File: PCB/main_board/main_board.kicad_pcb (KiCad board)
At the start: 4 copper layers, 55.3 x 29 mm, 56 parts, among them CN1 XT30PW-M, CN2 XT30PW-M, U1 XT30PW-F, U2 W25Q32JVUUIQ, U3 W25N01GVZEIG_C907680, U4 INA226, U5 INA226, U6 RP2040, U7 AZ1117-3.3, X1 X322512MSB4SI

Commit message: Ready to JLC
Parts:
- added G***: LOGO, pcb_lib:OpenSourceHardware_3.5mm, F.Cu at (60.4, 27.0)
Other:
- board text added: "SC+Battery Current Sensor Board Author: Kelvin Zhao Version: V0.1 Design Date: Feb 2024"
- board text added: "SDA-BAT"
- board text added: "SDA-CAP"
- board text removed: "USB-C"

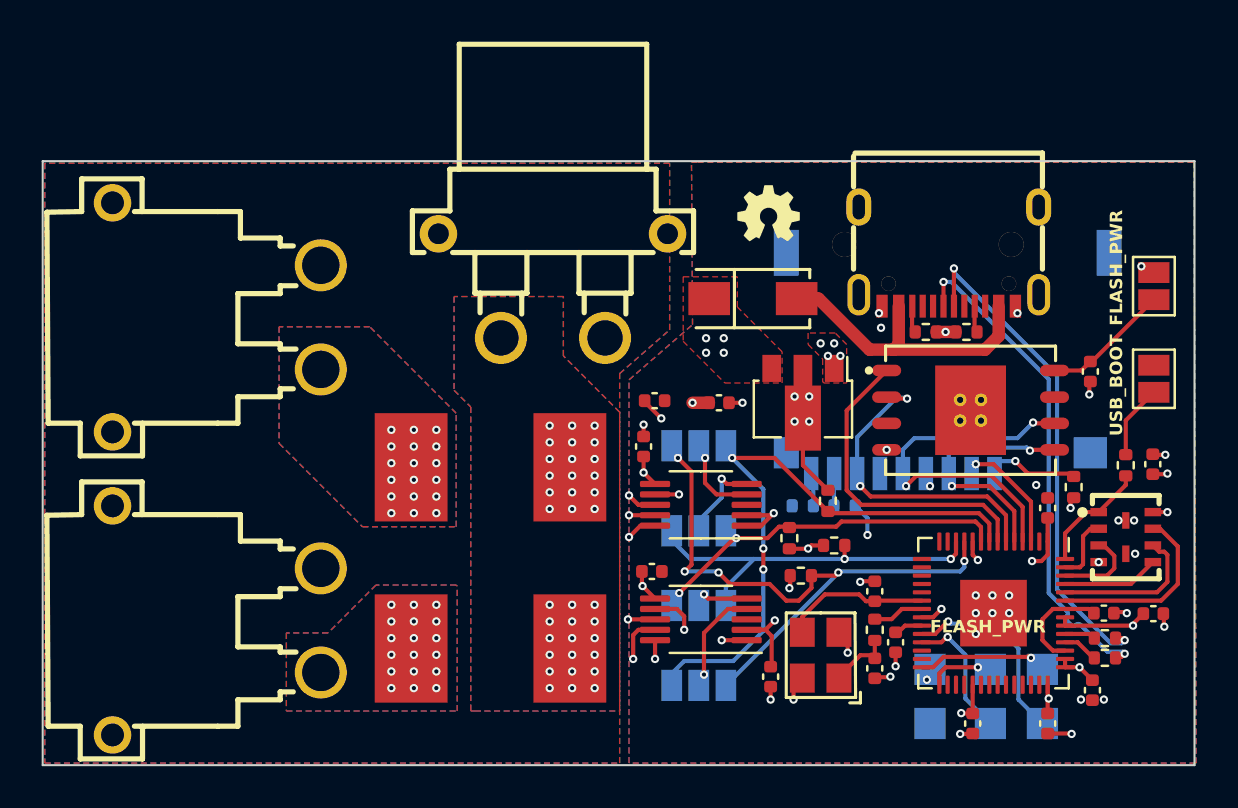
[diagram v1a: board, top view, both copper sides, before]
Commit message: Change LDO to BUCK converter
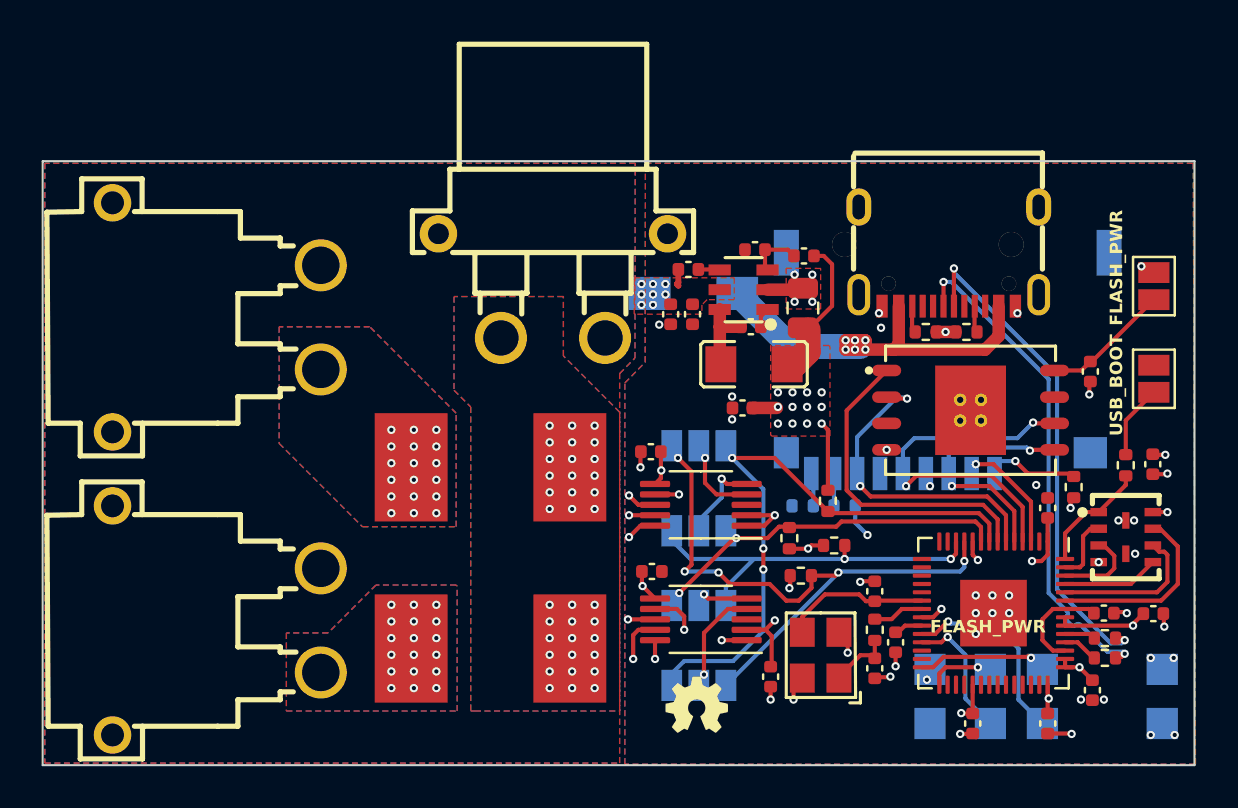
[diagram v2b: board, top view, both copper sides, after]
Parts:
- added C18: 0.1u, Capacitor_SMD:C_0402_1005Metric, F.Cu at (59.5, 32.5)
- added C19: 22u, Capacitor_SMD:C_0805_2012Metric, F.Cu at (62.0, 31.6)
- added C4: 0.1u, Capacitor_SMD:C_0402_1005Metric, F.Cu at (55.6, 31.9)
- added L1: CMP321609XD6R8MT, pcb_lib:L1206, F.Cu at (59.6, 34.2)
- added R3: 10k, Capacitor_SMD:C_0402_1005Metric, F.Cu at (56.5, 29.7)
- added R4: 51k, Capacitor_SMD:C_0402_1005Metric, F.Cu at (62.0, 29.1)
- added R5: 22.1k, Capacitor_SMD:C_0402_1005Metric, F.Cu at (59.7, 28.8)
- added TP7: 3.3, TestPoint:TestPoint_Pad_1.5x1.5mm, B.Cu at (79.2, 51.5)
- added TP8: GND, TestPoint:TestPoint_Pad_1.5x1.5mm, B.Cu at (79.2, 48.9)
- D1: moved to B.Cu
- U7: value AZ1117-3.3 -> TPS560430XDBVR; footprint Package_TO_SOT_SMD:SOT-89-3 -> pcb_lib:SOT-23-6_L2.9-W1.6-P0.95-LS2.8-BL
- moved G*** 23.9 mm to (56.9, 50.6)
- moved U7 6.40 mm to (59.2, 30.7), turned to 90 degrees
- moved C3 4.44 mm to (56.7, 31.9), turned to 90 degrees
- moved C12 4.23 mm to (59.1, 36.4), turned to 180 degrees
- moved D1 2.86 mm to (56.8, 30.9)
- moved C14 0.43 mm to (54.7, 38.5), turned to 180 degrees
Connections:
- C3 pad 1: IBAT+ -> GND
- C3 pad 2: GND -> IBAT+
- R14 pad 1: GND -> +3.3V
- U7 pad 1: GND -> Net-(U7-CB)
- U7 pad 2: +3.3V -> GND
- U7 pad 3: IBAT+ -> Net-(U7-FB)
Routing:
- net GND: track 45.5 -> 21.5 mm, vias 43 -> 46
- net VBUS: track 14.6 -> 20.1 mm, vias 0 -> 6
- net +3.3V: track 33.9 -> 39.2 mm, vias 22 -> 32
- net IBAT+: track 54.4 -> 50.0 mm, vias 25 -> 28
- net Net-(U7-SW): track 0.00 -> 3.64 mm
- net Net-(U7-FB): track 0.00 -> 2.39 mm
- net Net-(U7-EN): track 0.00 -> 1.03 mm
- net Net-(U7-CB): track 0.00 -> 0.96 mm
- added copper zone on F.Cu, net +3.3V
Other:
- board text added: "3V3"

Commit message: Ready for JLC for second time
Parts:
- moved G*** 0.92 mm to (56.1, 51.0)
- moved C12 0.80 mm to (59.0, 37.1)
- moved D1 0.76 mm to (57.5, 31.0)
- moved L1 0.65 mm to (59.6, 34.9)
- moved R5 0.32 mm to (59.8, 28.4)
- moved C18 0.30 mm to (59.5, 32.8)
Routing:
- net VBUS: track 20.1 -> 19.2 mm
- net Net-(U7-FB): track 2.39 -> 2.99 mm
- net +3.3V: track 39.2 -> 39.3 mm, vias 32 -> 28
- net IBAT+: vias 28 -> 25
- net GND: vias 46 -> 45
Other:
- board text added: "Open Source Hardware"

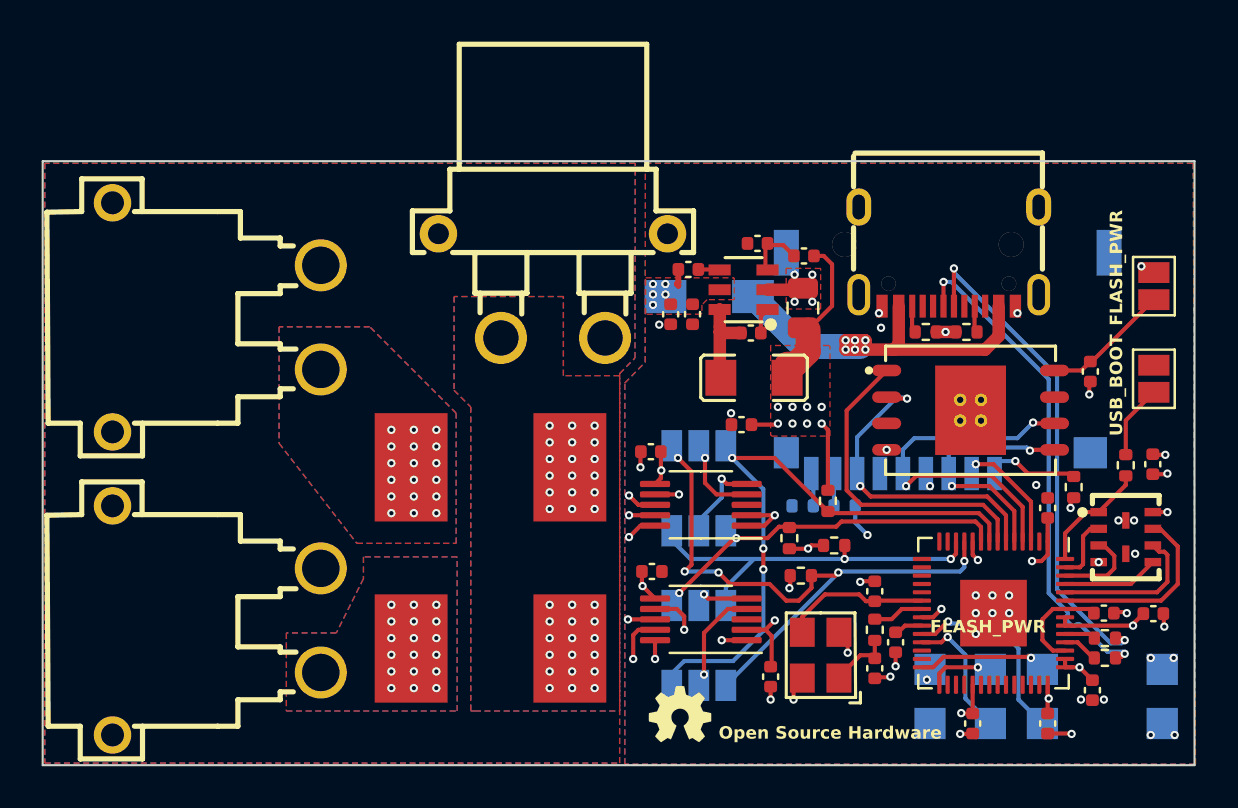
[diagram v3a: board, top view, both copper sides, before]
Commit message: Remove extra current carrier
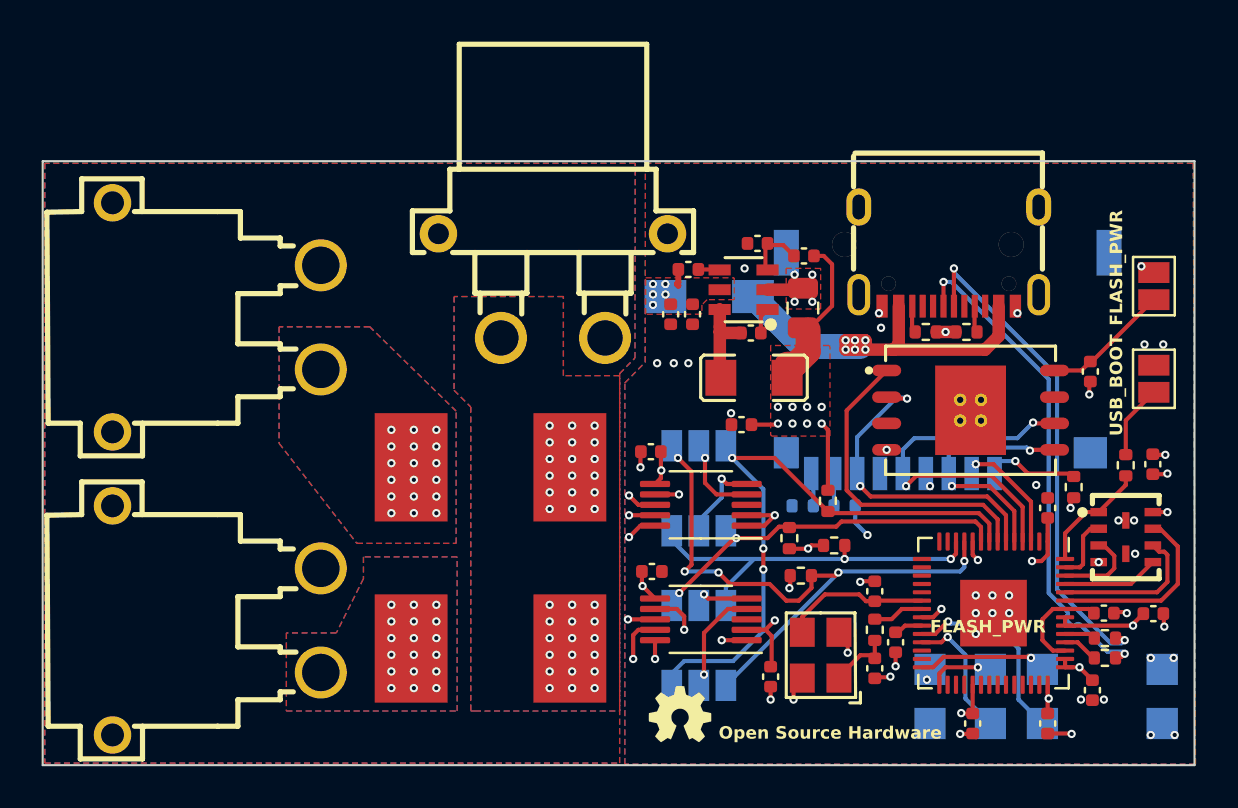
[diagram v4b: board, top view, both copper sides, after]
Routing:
- net GND: track 21.5 -> 31.3 mm, vias 45 -> 50
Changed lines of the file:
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@@
   (via (at 68.85 32.7) (size 0.4) (drill 0.2) (layers "F.Cu" "B.Cu") (free) (net 2))
   (via (at 66.45 48.75) (size 0.4) (drill 0.2) (layers "F.Cu" "B.Cu") (free) (net 2))
+  (via (at 56.5 34.2) (size 0.4) (drill 0.2) (layers "F.Cu" "B.Cu") (net 2))
   (via (at 58.55 36.6) (size 0.4) (drill 0.2) (layers "F.Cu" "B.Cu") (free) (net 2))
   (via (at 73.2 40.05) (size 0.4) (drill 0.2) (layers "F.Cu" "B.Cu") (free) (net 2))
   (via (at 79.4 38.6) (size 0.4) (drill 0.2) (layers "F.Cu" "B.Cu") (free) (net 2))
   (via (at 77.9 41.75) (size 0.4) (drill 0.2) (layers "F.Cu" "B.Cu") (free) (net 2))
+  (via (at 78.4 33.3) (size 0.4) (drill 0.2) (layers "F.Cu" "B.Cu") (free) (net 2))
   (via (at 71.9 46.2) (size 0.4) (drill 0.2) (layers "F.Cu" "B.Cu") (net 2))
   (via (at 75.75 35.7) (size 0.4) (drill 0.2) (layers "F.Cu" "B.Cu") (free) (net 2))
@@
   (via (at 56.3 47) (size 0.4) (drill 0.2) (layers "F.Cu" "B.Cu") (free) (net 2))
   (via (at 74.9 52) (size 0.4) (drill 0.2) (layers "F.Cu" "B.Cu") (free) (net 2))
+  (via (at 59.2 29.65) (size 0.4) (drill 0.2) (layers "F.Cu" "B.Cu") (free) (net 2))
   (via (at 67.95 49.4) (size 0.4) (drill 0.2) (layers "F.Cu" "B.Cu") (net 2))
   (via (at 66.02 38.36) (size 0.4) (drill 0.2) (layers "F.Cu" "B.Cu") (net 2))
@@
   (via (at 70.3 45.35) (size 0.4) (drill 0.2) (layers "F.Cu" "B.Cu") (net 2))
   (via (at 60.65 41.5) (size 0.4) (drill 0.2) (layers "F.Cu" "B.Cu") (free) (net 2))
-  (via (at 55.1 32.35) (size 0.4) (drill 0.2) (layers "F.Cu" "B.Cu") (net 2))
+  (via (at 55 34.2) (size 0.4) (drill 0.2) (layers "F.Cu" "B.Cu") (net 2))
   (via (at 78.7 48.35) (size 0.4) (drill 0.2) (layers "F.Cu" "B.Cu") (net 2))
   (via (at 65.75 32.5) (size 0.4) (drill 0.2) (layers "F.Cu" "B.Cu") (free) (net 2))
@@
   (via (at 61.6 31.25) (size 0.4) (drill 0.2) (layers "F.Cu" "B.Cu") (free) (net 2))
   (via (at 70.3 46.2) (size 0.4) (drill 0.2) (layers "F.Cu" "B.Cu") (net 2))
+  (via (at 79.3 33.3) (size 0.4) (drill 0.2) (layers "F.Cu" "B.Cu") (free) (net 2))
+  (via (at 55.8 34.2) (size 0.4) (drill 0.2) (layers "F.Cu" "B.Cu") (net 2))
   (via (at 79.35 46.85) (size 0.4) (drill 0.2) (layers "F.Cu" "B.Cu") (net 2))
+  (segment (start 52.5 32.9875) (end 59.8625 32.9875) (width 1.2) (layer "In1.Cu") (net 2))
+  (segment (start 59.8625 32.9875) (end 61.6 31.25) (width 1.2) (layer "In1.Cu") (net 2))
   (segment (start 39.2525 43.65) (end 38.8525 44.05) (width 0.2) (layer "In1.Cu") (net 2))
   (segment (start 55.95 30.4) (end 56 30.4) (width 0.286004) (layer "F.Cu") (net 3))
@@
         (xy 40.583332 42.85)
         (xy 45.35 42.85)
-        (xy 45.35 36.6)
+        (xy 45.35 36.5)
         (xy 41.2 32.45)
       )

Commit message: Add Custom ID
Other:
- board text added: "JLCJLCJLCJLC"
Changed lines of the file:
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@@
+    (effects (font (size 0.6 0.6) (thickness 0.1) bold) (justify left bottom mirror))
+  )
+  (gr_text "JLCJLCJLCJLC" (at 72.15 26.75) (layer "B.SilkS")
     (effects (font (size 0.6 0.6) (thickness 0.1) bold) (justify left bottom mirror))
   )

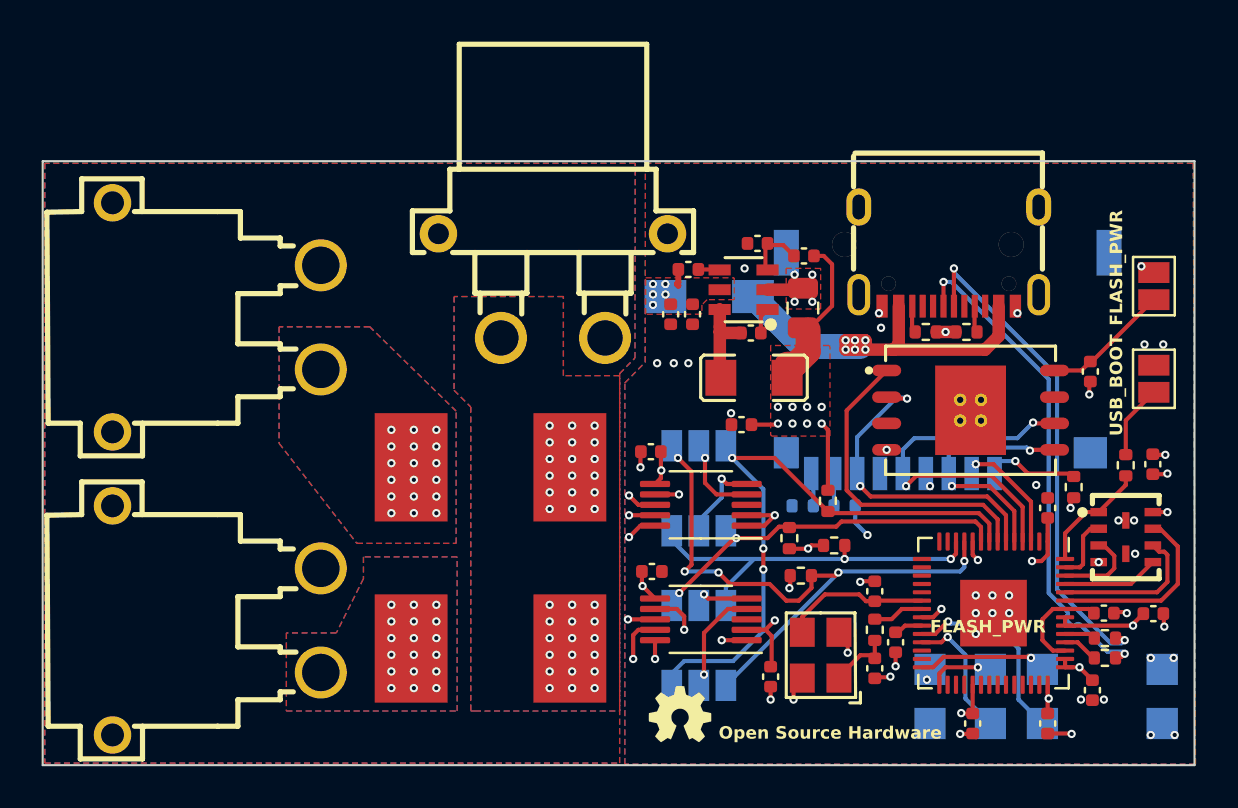
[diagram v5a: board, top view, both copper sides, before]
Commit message: Change vias drills to 0.3/0.5mm
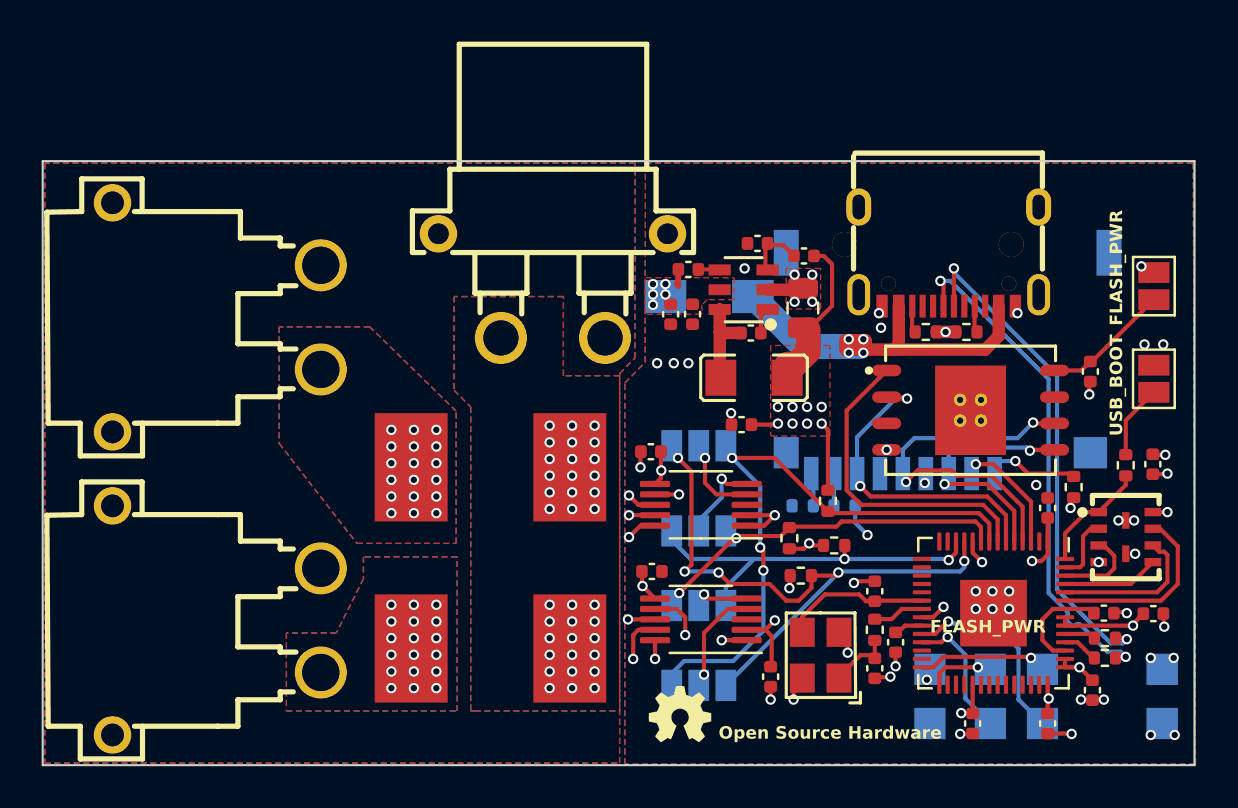
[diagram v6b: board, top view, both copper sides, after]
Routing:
- net GND: track 31.3 -> 31.9 mm, vias 50 -> 49
- net VBUS: vias 6 -> 4

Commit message: Change INA226 package for SMT
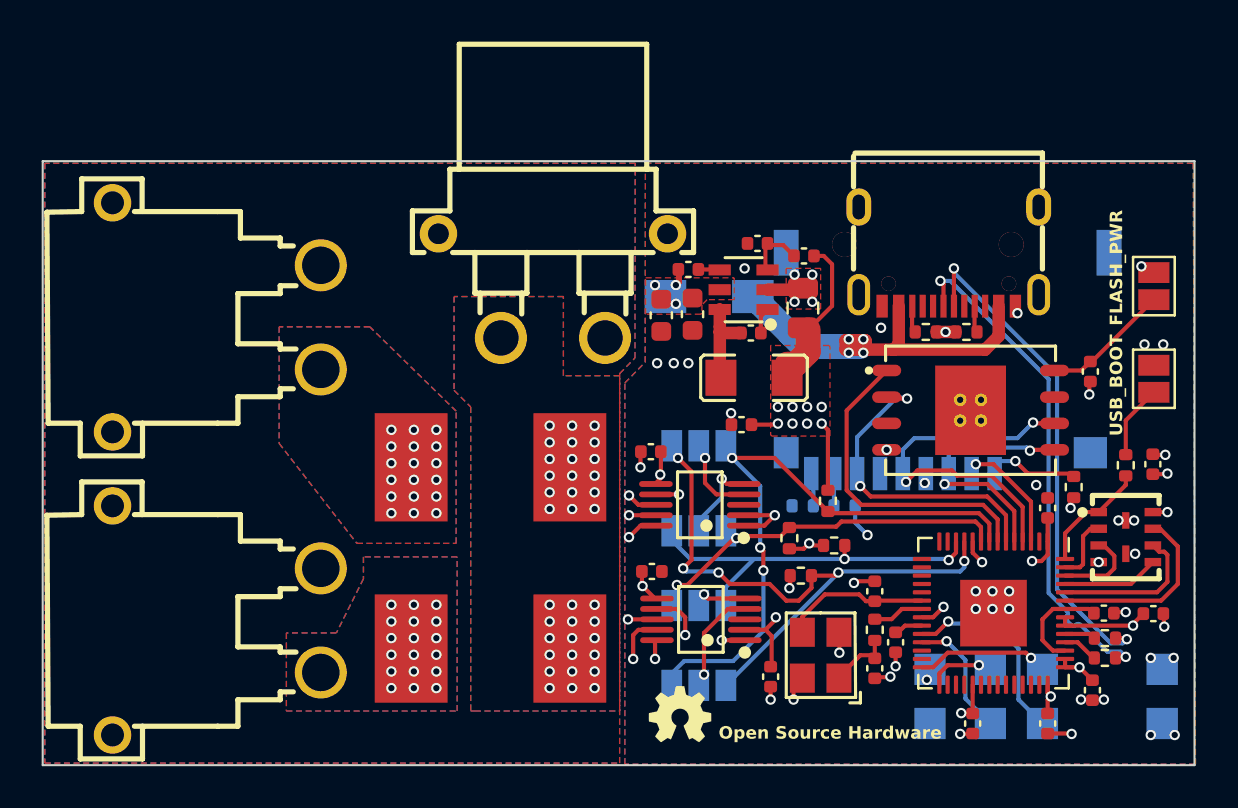
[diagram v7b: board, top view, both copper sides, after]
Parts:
- C3, C4: footprint Capacitor_SMD:C_0402_1005Metric -> Capacitor_SMD:C_0603_1608Metric
- U4, U5: footprint Package_SO:VSSOP-10_3x3mm_P0.5mm -> pcb_lib:MSOP-10_L3.0-W3.0-P0.50-LS5.0-BL
- moved C3 1.50 mm to (55.2, 31.9)
- moved C4 1.05 mm to (56.7, 31.9)
- moved U4 0.05 mm to (57.0, 41.0), turned to 90 degrees
- turned U5 to 90 degrees
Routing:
- net SCL1: track 16.7 -> 17.8 mm
- net GND: track 31.9 -> 31.6 mm, vias 49 -> 48
- net IBAT+: track 50.0 -> 50.2 mm, vias 25 -> 23
